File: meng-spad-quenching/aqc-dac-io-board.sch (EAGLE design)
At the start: 41 parts, among them IC1 LT1366, IC2 74LVT126, IC3 MAX1680, X1 CONN_VREF_CASCODE_IBIAS, X2 CONN_VREF_DIAMOND_IBIAS, X3 CONN_VREF_ONE_SHOT, X4 CONN_FORCE_QUENCH, X5 CONN_PHOTON_COUNTER

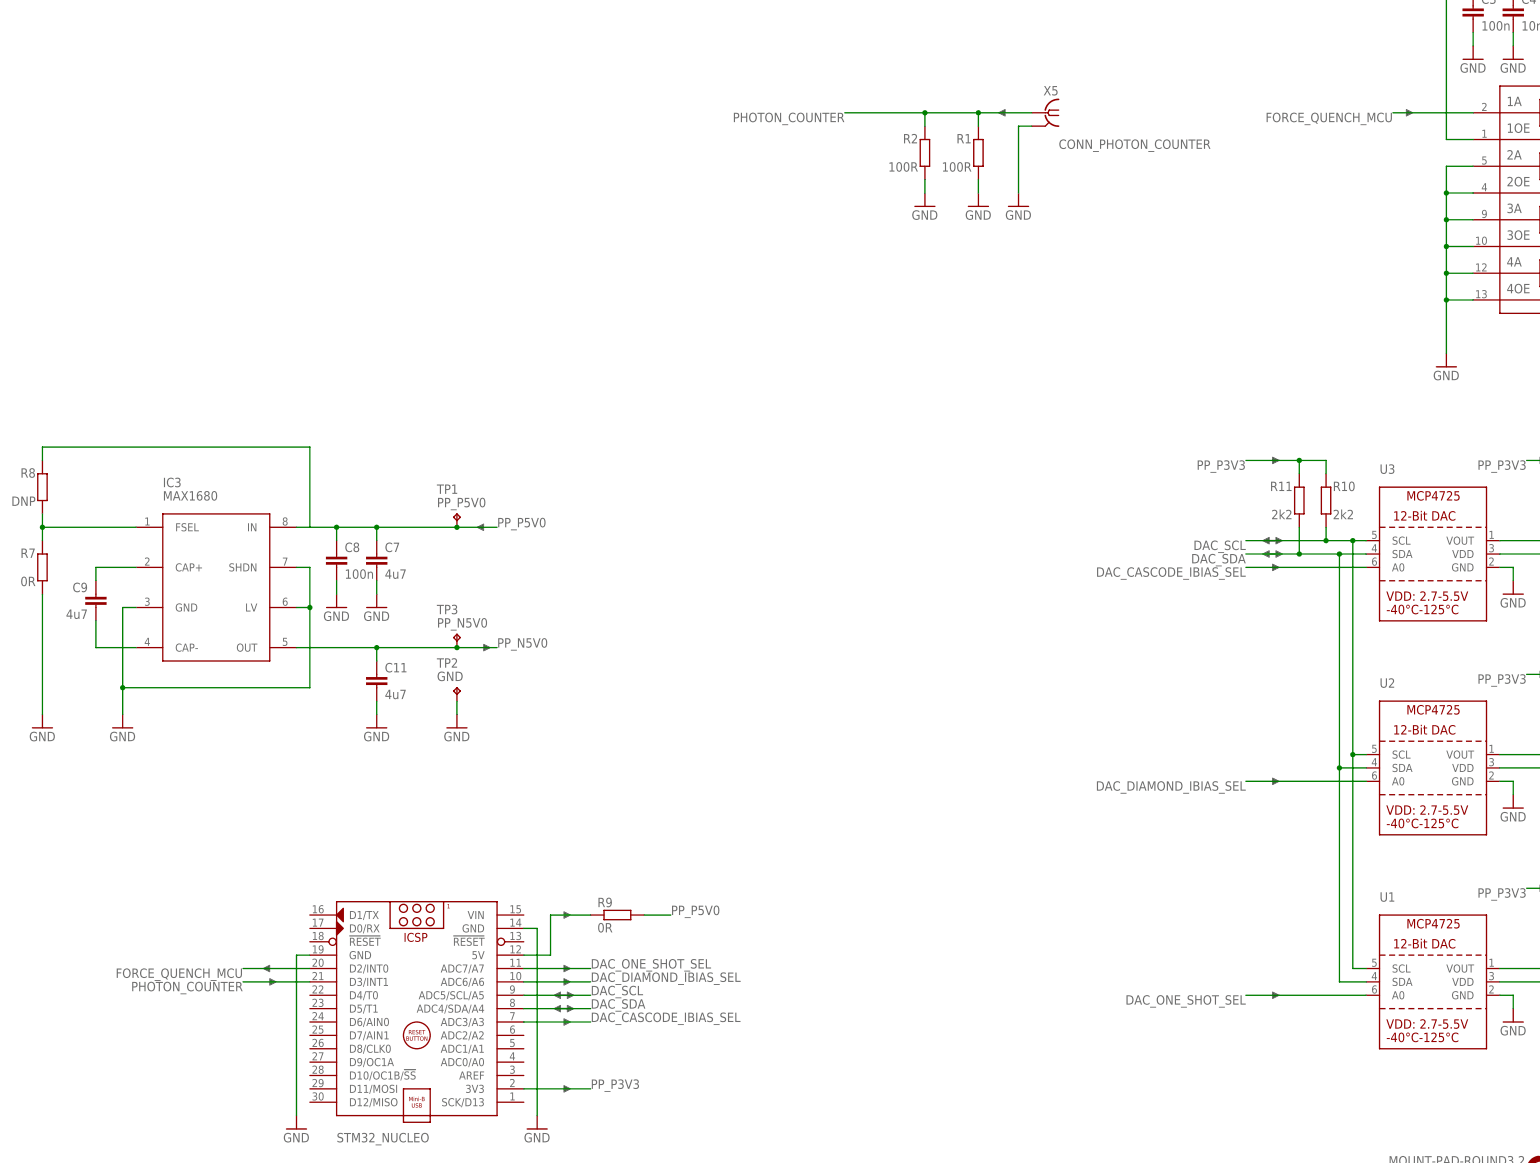
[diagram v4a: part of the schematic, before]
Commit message: Added debounced trigger switch, routed, and exported gerbers
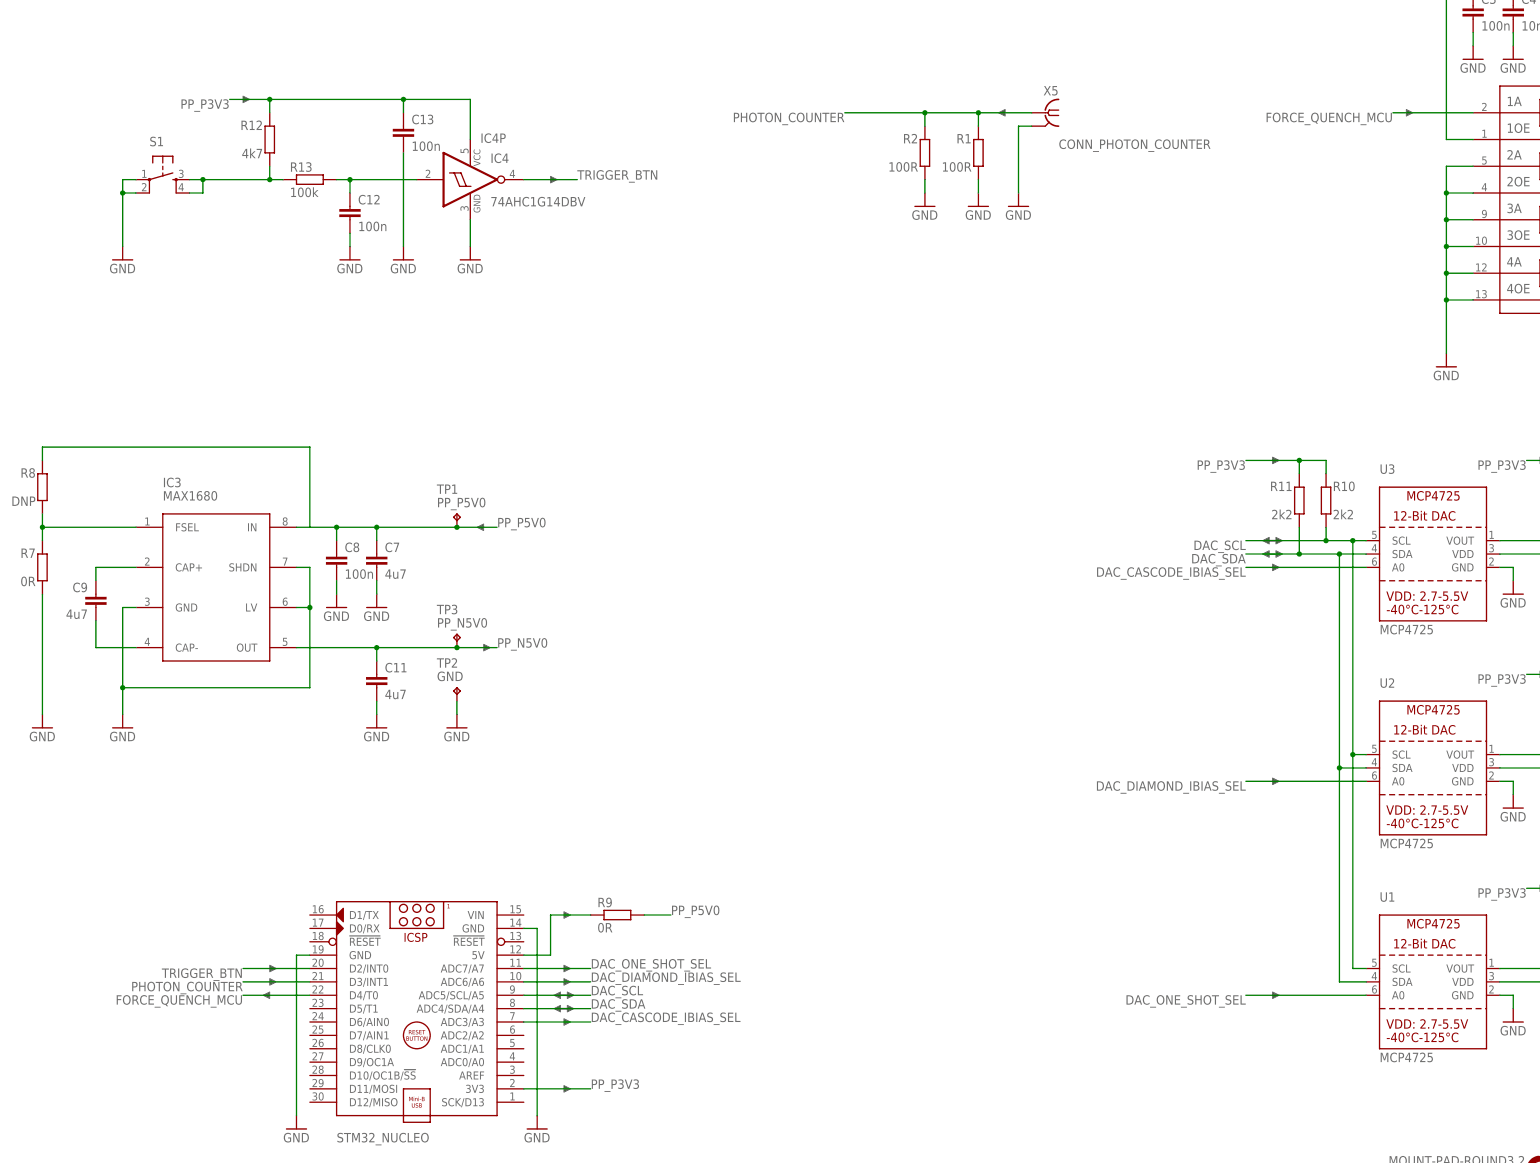
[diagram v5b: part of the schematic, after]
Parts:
- added C12, C13: 100n, rcl:C-EUC0603
- added IC4: 74AHC1G14DBV, 74xx-little-us:74AHC1G14DBV
- added R12: 4k7, resistor:R-EU_R0603
- added R13: 100k, resistor:R-EU_R0603
- added S1: (no value), Kramnik's Library:TAC_SWITCHPTH
- U1, U2, U3: value (none) -> MCP4725
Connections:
- new net N$11: R12.1, R13.2, S1.3, S1.4
- new net N$12: C12.1, IC4A.I, R13.1
- new net TRIGGER_BTN: IC4A.O, STM32_NUCLEO.D2/INT0
- net FORCE_QUENCH_MCU: now also STM32_NUCLEO.D4/T0; no longer STM32_NUCLEO.D2/INT0
- net GND: now also C12.2, C13.2, IC4P.GND, S1.1, S1.2
- net PP_P3V3: now also C13.1, IC4P.VCC, R12.2
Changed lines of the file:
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@@
 <setting verticaltext="up"/>
 </settings>
-<grid distance="0.1" unitdist="inch" unit="inch" style="lines" multiple="1" display="no" altdistance="0.01" altunitdist="inch" altunit="inch"/>
+<grid distance="0.1" unitdist="inch" unit="inch" style="lines" multiple="1" display="yes" altdistance="0.01" altunitdist="inch" altunit="inch"/>
 <layers>
 <layer number="1" name="Top" color="4" fill="1" visible="no" active="no"/>
@@
 </classes>
 <parts>
-<part name="U3" library="microbuilder" deviceset="DAC_MCP4725" device=""/>
-<part name="U2" library="microbuilder" deviceset="DAC_MCP4725" device=""/>
-<part name="U1" library="microbuilder" deviceset="DAC_MCP4725" device=""/>
+<part name="U3" library="microbuilder" deviceset="DAC_MCP4725" device="" value="MCP4725"/>
+<part name="U2" library="microbuilder" deviceset="DAC_MCP4725" device="" value="MCP4725"/>
+<part name="U1" library="microbuilder" deviceset="DAC_MCP4725" device="" value="MCP4725"/>
 <part name="X1" library="con-coax" deviceset="SMA-" device="142-0701-801/806" value="CONN_VREF_CASCODE_IBIAS"/>
 <part name="X2" library="con-coax" deviceset="SMA-" device="142-0701-801/806" value="CONN_VREF_DIAMOND_IBIAS"/>
@@
 <part name="R2" library="resistor" deviceset="R-EU_" device="R0603" value="100R"/>
 <part name="GND26" library="supply1" deviceset="GND" device=""/>
+<part name="S1" library="Kramnik's Library" deviceset="TAC_SWITCH" device="PTH"/>
+<part name="GND27" library="supply1" deviceset="GND" device=""/>
+<part name="R12" library="resistor" deviceset="R-EU_" device="R0603" value="4k7"/>
+<part name="R13" library="resistor" deviceset="R-EU_" device="R0603" value="100k"/>
+<part name="C12" library="rcl" deviceset="C-EU" device="C0603" value="100n"/>
+<part name="GND29" library="supply1" deviceset="GND" device=""/>
+<part name="IC4" library="74xx-little-us" deviceset="74*1G14" device="DBV" technology="AHC"/>
+<part name="GND30" library="supply1" deviceset="GND" device=""/>
+<part name="C13" library="rcl" deviceset="C-EU" device="C0603" value="100n"/>
+<part name="GND31" library="supply1" deviceset="GND" device=""/>
+<part name="DNP21" library="meng" deviceset="ARROW_1DIR" device=""/>
+<part name="DNP22" library="meng" deviceset="ARROW_1DIR" device=""/>
+<part name="U$5" library="Kramnik's Library" deviceset="LEFT_ARROW" device=""/>
 </parts>
 <sheets>
@@
 </instance>
 <instance part="U$3" gate="G$1" x="68.58" y="71.12" rot="R180"/>
-<instance part="U$4" gate="G$1" x="68.58" y="73.66"/>
+<instance part="U$4" gate="G$1" x="68.58" y="73.66" rot="R180"/>
 <instance part="DNP18" gate="G$1" x="124.46" y="73.66" smashed="yes"/>
 <instance part="DNP19" gate="G$1" x="124.46" y="71.12" smashed="yes"/>
@@
 </instance>
 <instance part="GND26" gate="1" x="193.04" y="218.44"/>
+<instance part="S1" gate="S" x="48.26" y="223.52"/>
+<instance part="GND27" gate="1" x="40.64" y="208.28" smashed="yes">
+<attribute name="VALUE" x="38.1" y="205.74" size="1.778" layer="96"/>
+</instance>
+<instance part="R12" gate="G$1" x="68.58" y="231.14" smashed="yes" rot="R90">
+<attribute name="NAME" x="67.31" y="234.7214" size="1.778" layer="95" rot="R180"/>
+<attribute name="VALUE" x="67.31" y="229.362" size="1.778" layer="96" rot="R180"/>
+</instance>
+<instance part="R13" gate="G$1" x="76.2" y="223.52" smashed="yes" rot="R180">
+<attribute name="NAME" x="72.39" y="225.0186" size="1.778" layer="95"/>
+<attribute name="VALUE" x="72.39" y="220.218" size="1.778" layer="96"/>
+</instance>
+<instance part="C12" gate="G$1" x="83.82" y="218.44" smashed="yes">
+<attribute name="NAME" x="85.344" y="218.821" size="1.778" layer="95"/>
+<attribute name="VALUE" x="85.344" y="213.741" size="1.778" layer="96"/>
+</instance>
+<instance part="GND29" gate="1" x="83.82" y="208.28" smashed="yes">
+<attribute name="VALUE" x="81.28" y="205.74" size="1.778" layer="96"/>
+</instance>
+<instance part="IC4" gate="A" x="106.68" y="223.52" smashed="yes">
+<attribute name="NAME" x="110.49" y="226.695" size="1.778" layer="95" font="vector"/>
+<attribute name="VALUE" x="110.49" y="218.44" size="1.778" layer="96" font="vector"/>
+</instance>
+<instance part="IC4" gate="P" x="106.68" y="223.52" smashed="yes">
+<attribute name="NAME" x="108.585" y="230.505" size="1.778" layer="95"/>
+</instance>
+<instance part="GND30" gate="1" x="106.68" y="208.28" smashed="yes">
+<attribute name="VALUE" x="104.14" y="205.74" size="1.778" layer="96"/>
+</instance>
+<instance part="C13" gate="G$1" x="93.98" y="233.68" smashed="yes">
+<attribute name="NAME" x="95.504" y="234.061" size="1.778" layer="95"/>
+<attribute name="VALUE" x="95.504" y="228.981" size="1.778" layer="96"/>
+</instance>
+<instance part="GND31" gate="1" x="93.98" y="208.28" smashed="yes">
+<attribute name="VALUE" x="91.44" y="205.74" size="1.778" layer="96"/>
+</instance>
+<instance part="DNP21" gate="G$1" x="63.5" y="238.76" smashed="yes"/>
+<instance part="DNP22" gate="G$1" x="121.92" y="223.52" smashed="yes"/>
+<instance part="U$5" gate="G$1" x="68.58" y="68.58"/>
 </instances>
 <busses>
@@
 <wire x1="193.04" y1="220.98" x2="193.04" y2="223.52" width="0.1524" layer="91"/>
 </segment>
+<segment>
+<pinref part="S1" gate="S" pin="1"/>
+<wire x1="43.18" y1="223.52" x2="40.64" y2="223.52" width="0.1524" layer="91"/>
+<wire x1="40.64" y1="223.52" x2="40.64" y2="220.98" width="0.1524" layer="91"/>
+<pinref part="S1" gate="S" pin="2"/>
+<wire x1="40.64" y1="220.98" x2="43.18" y2="220.98" width="0.1524" layer="91"/>
+<pinref part="GND27" gate="1" pin="GND"/>
+<wire x1="40.64" y1="210.82" x2="40.64" y2="220.98" width="0.1524" layer="91"/>
+<junction x="40.64" y="220.98"/>
+</segment>
+<segment>
+<pinref part="C12" gate="G$1" pin="2"/>
+<pinref part="GND29" gate="1" pin="GND"/>
+<wire x1="83.82" y1="213.36" x2="83.82" y2="210.82" width="0.1524" layer="91"/>
+</segment>
+<segment>
+<pinref part="GND30" gate="1" pin="GND"/>
+<pinref part="IC4" gate="P" pin="GND"/>
+<wire x1="106.68" y1="210.82" x2="106.68" y2="215.9" width="0.1524" layer="91"/>
+</segment>
+<segment>
+<pinref part="C13" gate="G$1" pin="2"/>
+<pinref part="GND31" gate="1" pin="GND"/>
+<wire x1="93.98" y1="228.6" x2="93.98" y2="210.82" width="0.1524" layer="91"/>
+</segment>
 </net>
 <net name="PHOTON_COUNTER" class="0">
@@
 <label x="307.34" y="88.9" size="1.778" layer="95" rot="R180"/>
 </segment>
+<segment>
+<pinref part="R12" gate="G$1" pin="2"/>
+<wire x1="68.58" y1="236.22" x2="68.58" y2="238.76" width="0.1524" layer="91"/>
+<wire x1="68.58" y1="238.76" x2="60.96" y2="238.76" width="0.1524" layer="91"/>
+<label x="60.96" y="238.76" size="1.778" layer="95" rot="R180"/>
+<wire x1="68.58" y1="238.76" x2="93.98" y2="238.76" width="0.1524" layer="91"/>
+<pinref part="IC4" gate="P" pin="VCC"/>
+<wire x1="93.98" y1="238.76" x2="106.68" y2="238.76" width="0.1524" layer="91"/>
+<wire x1="106.68" y1="238.76" x2="106.68" y2="231.14" width="0.1524" layer="91"/>
+<junction x="68.58" y="238.76"/>
+<pinref part="C13" gate="G$1" pin="1"/>
+<wire x1="93.98" y1="236.22" x2="93.98" y2="238.76" width="0.1524" layer="91"/>
+<junction x="93.98" y="238.76"/>
+</segment>
 </net>
 <net name="FORCE_QUENCH_MCU" class="0">
@@
 </segment>
 <segment>
-<pinref part="STM32_NUCLEO" gate="G$1" pin="D2/INT0"/>
-<wire x1="76.2" y1="73.66" x2="63.5" y2="73.66" width="0.1524" layer="91"/>
-<label x="63.5" y="73.66" size="1.778" layer="95" rot="R180"/>
+<pinref part="STM32_NUCLEO" gate="G$1" pin="D4/T0"/>
+<wire x1="76.2" y1="68.58" x2="63.5" y2="68.58" width="0.1524" layer="91"/>
+<label x="63.5" y="68.58" size="1.778" layer="95" rot="R180"/>
 </segment>
 </net>
@@
 </segment>
 </net>
+<net name="N$11" class="0">
+<segment>
+<pinref part="S1" gate="S" pin="4"/>
+<wire x1="53.34" y1="220.98" x2="55.88" y2="220.98" width="0.1524" layer="91"/>
+<wire x1="55.88" y1="220.98" x2="55.88" y2="223.52" width="0.1524" layer="91"/>
+<pinref part="S1" gate="S" pin="3"/>
+<wire x1="55.88" y1="223.52" x2="53.34" y2="223.52" width="0.1524" layer="91"/>
+<wire x1="55.88" y1="223.52" x2="68.58" y2="223.52" width="0.1524" layer="91"/>
+<pinref part="R12" gate="G$1" pin="1"/>
+<wire x1="68.58" y1="223.52" x2="68.58" y2="226.06" width="0.1524" layer="91"/>
+<pinref part="R13" gate="G$1" pin="2"/>
+<wire x1="68.58" y1="223.52" x2="71.12" y2="223.52" width="0.1524" layer="91"/>
+<junction x="68.58" y="223.52"/>
+<junction x="55.88" y="223.52"/>
+</segment>
+</net>
+<net name="N$12" class="0">
+<segment>
+<pinref part="R13" gate="G$1" pin="1"/>
+<wire x1="81.28" y1="223.52" x2="83.82" y2="223.52" width="0.1524" layer="91"/>
+<pinref part="C12" gate="G$1" pin="1"/>
+<wire x1="83.82" y1="223.52" x2="83.82" y2="220.98" width="0.1524" layer="91"/>
+<wire x1="83.82" y1="223.52" x2="96.52" y2="223.52" width="0.1524" layer="91"/>
+<junction x="83.82" y="223.52"/>
+<pinref part="IC4" gate="A" pin="I"/>
+</segment>
+</net>
+<net name="TRIGGER_BTN" class="0">
+<segment>
+<pinref part="IC4" gate="A" pin="O"/>
+<wire x1="116.84" y1="223.52" x2="127" y2="223.52" width="0.1524" layer="91"/>
+<label x="127" y="223.52" size="1.778" layer="95"/>
+</segment>
+<segment>
+<pinref part="STM32_NUCLEO" gate="G$1" pin="D2/INT0"/>
+<wire x1="76.2" y1="73.66" x2="63.5" y2="73.66" width="0.1524" layer="91"/>
+<label x="63.5" y="73.66" size="1.778" layer="95" rot="R180"/>
+</segment>
+</net>
